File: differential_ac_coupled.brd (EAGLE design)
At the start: 66 x 40.6 mm, 25 parts, among them U1 AD8421

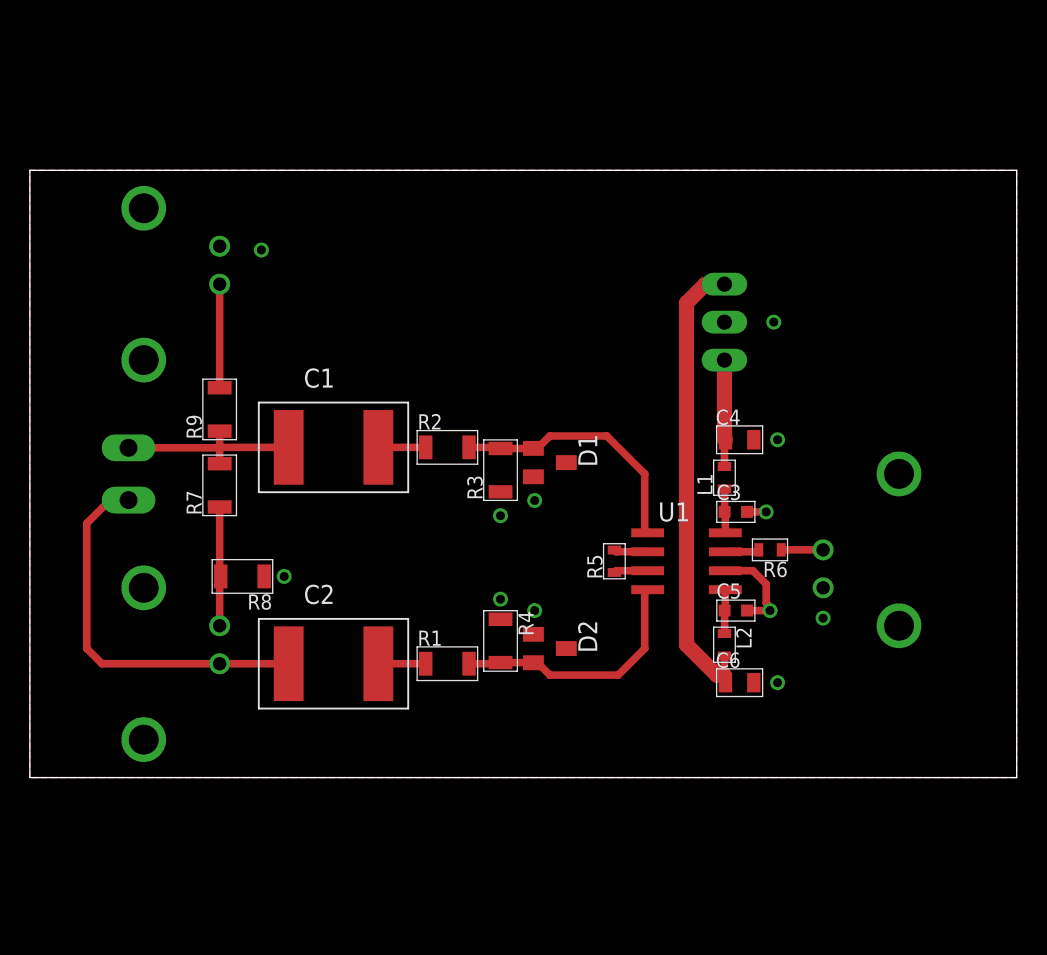
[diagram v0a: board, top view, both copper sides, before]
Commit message: Add battery holders
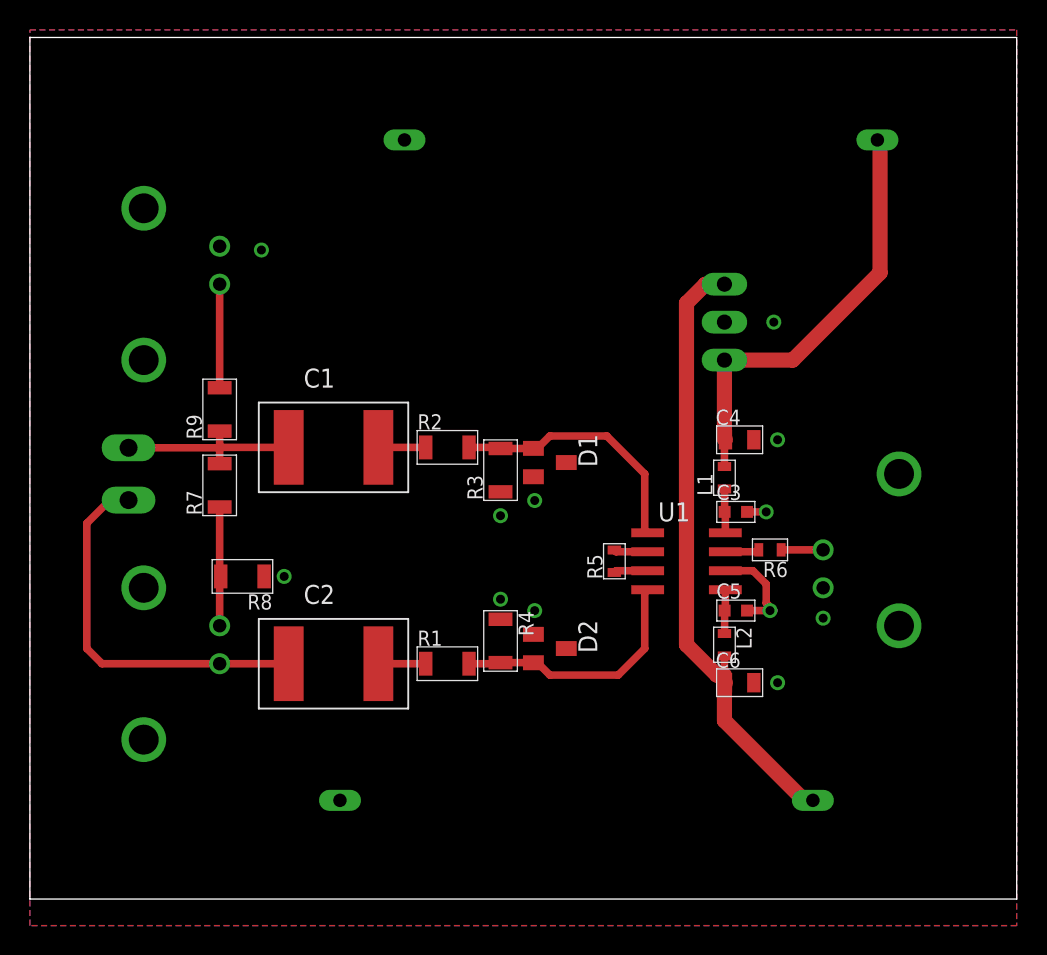
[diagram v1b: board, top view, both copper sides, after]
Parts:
- added U$1, U$2: BATT-HOLDER, regulator-jqi:BH23A-BATT-HOLDER
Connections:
- net GND: now also U$1.P$2-, U$2.P$1+
- net V+: now also U$1.P$1+
- net V-: now also U$2.P$2-
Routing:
- net V+: track 7.18 -> 29.0 mm
- net V-: track 31.1 -> 41.8 mm
- net GND: vias 2 -> 11
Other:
- board size 66 x 40.6 mm -> 66 x 57.7 mm
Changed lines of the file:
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@@
 <?xml version="1.0" encoding="utf-8"?>
 <!DOCTYPE eagle SYSTEM "eagle.dtd">
-<eagle version="6.6.0">
+<eagle version="6.5.0">
 <drawing>
 <settings>
@@
 <board>
 <plain>
-<wire x1="0" y1="40.64" x2="0" y2="0" width="0" layer="20"/>
-<wire x1="0" y1="0" x2="66.04" y2="0" width="0" layer="20"/>
-<wire x1="66.04" y1="0" x2="66.04" y2="40.64" width="0" layer="20"/>
-<wire x1="66.04" y1="40.64" x2="0" y2="40.64" width="0" layer="20"/>
+<wire x1="0" y1="49.53" x2="0" y2="-8.128" width="0" layer="20"/>
+<wire x1="0" y1="-8.128" x2="66.04" y2="-8.128" width="0" layer="20"/>
+<wire x1="66.04" y1="-8.128" x2="66.04" y2="49.53" width="0" layer="20"/>
+<wire x1="66.04" y1="49.53" x2="0" y2="49.53" width="0" layer="20"/>
 </plain>
 <attributes>
@@
 <element name="R8" library="jqi_passives" package="R_1206" value="" x="14.224" y="13.462" rot="R180"/>
 <element name="R9" library="jqi_passives" package="R_1206" value="0R" x="12.7" y="24.638" rot="R90"/>
+<element name="U$1" library="regulator-jqi" package="BH23A-BATT-HOLDER" value="BATT-HOLDER" x="40.894" y="42.672" rot="MR0">
+<attribute name="DIGIKEY" value="BH23APC-ND" x="40.894" y="42.672" size="1.778" layer="28" rot="MR0" display="off"/>
+</element>
+<element name="U$2" library="regulator-jqi" package="BH23A-BATT-HOLDER" value="BATT-HOLDER" x="36.576" y="-1.524" rot="MR180">
+<attribute name="DIGIKEY" value="BH23APC-ND" x="36.576" y="-1.524" size="1.778" layer="28" rot="MR180" display="off"/>
+</element>
 </elements>
 <signals>
@@
 <contactref element="IN-" pad="2"/>
 <contactref element="R8" pad="P$1"/>
-<polygon width="0.254" layer="1" isolate="1.27" thermals="no">
-<vertex x="0" y="40.64"/>
-<vertex x="66.04" y="40.64"/>
-<vertex x="66.04" y="0"/>
-<vertex x="0" y="0"/>
+<polygon width="0.254" layer="1" isolate="1.27">
+<vertex x="0" y="50.038"/>
+<vertex x="66.04" y="50.038"/>
+<vertex x="66.04" y="-9.906"/>
+<vertex x="0" y="-9.906"/>
 </polygon>
 <wire x1="46.542" y1="13.843" x2="48.387" y2="13.843" width="0.508" layer="1"/>
@@
 <wire x1="47.994" y1="17.78" x2="49.276" y2="17.78" width="0.508" layer="1"/>
 <polygon width="0.4064" layer="16">
-<vertex x="0" y="40.64"/>
-<vertex x="66.04" y="40.64"/>
-<vertex x="66.04" y="0"/>
-<vertex x="0" y="0"/>
+<vertex x="0" y="50.038"/>
+<vertex x="66.04" y="50.038"/>
+<vertex x="66.04" y="-9.906"/>
+<vertex x="0" y="-9.906"/>
 </polygon>
 <via x="49.276" y="17.78" extent="1-16" drill="0.6"/>
 <via x="49.53" y="11.176" extent="1-16" drill="0.6"/>
+<contactref element="U$1" pad="P$2-"/>
+<contactref element="U$2" pad="P$1+"/>
+<via x="50.038" y="22.606" extent="1-16" drill="0.6"/>
+<via x="33.782" y="18.542" extent="1-16" drill="0.6"/>
+<via x="31.496" y="17.526" extent="1-16" drill="0.6"/>
+<via x="33.782" y="11.176" extent="1-16" drill="0.6"/>
+<via x="31.496" y="11.938" extent="1-16" drill="0.6"/>
+<via x="50.038" y="6.35" extent="1-16" drill="0.6"/>
+<via x="53.086" y="10.668" extent="1-16" drill="0.6"/>
+<via x="49.784" y="30.48" extent="1-16" drill="0.6"/>
+<via x="17.018" y="13.462" extent="1-16" drill="0.6"/>
 </signal>
 <signal name="N$7">
@@
 <wire x1="43.942" y1="31.75" x2="45.212" y2="33.02" width="1.016" layer="1"/>
 <wire x1="45.212" y1="33.02" x2="46.482" y2="33.02" width="1.016" layer="1"/>
+<contactref element="U$2" pad="P$2-"/>
+<wire x1="52.4002" y1="-1.524" x2="51.816" y2="-1.524" width="1.016" layer="1"/>
+<wire x1="51.816" y1="-1.524" x2="46.482" y2="3.81" width="1.016" layer="1"/>
+<wire x1="46.482" y1="3.81" x2="46.482" y2="6.284" width="1.016" layer="1"/>
+<wire x1="46.482" y1="6.284" x2="46.548" y2="6.35" width="1.016" layer="1"/>
 </signal>
 <signal name="V+">
@@
 <wire x1="46.482" y1="27.94" x2="46.482" y2="22.672" width="1.016" layer="1"/>
 <wire x1="46.482" y1="22.672" x2="46.548" y2="22.606" width="1.016" layer="1"/>
+<contactref element="U$1" pad="P$1+"/>
+<wire x1="46.482" y1="27.94" x2="51.054" y2="27.94" width="1.016" layer="1"/>
+<wire x1="51.054" y1="27.94" x2="56.896" y2="33.782" width="1.016" layer="1"/>
+<wire x1="56.896" y1="33.782" x2="56.896" y2="42.4942" width="1.016" layer="1"/>
+<wire x1="56.896" y1="42.4942" x2="56.7182" y2="42.672" width="1.016" layer="1"/>
 </signal>
 <signal name="N$5">
@@
 <wire x1="12.7" y1="13.388" x2="12.774" y2="13.462" width="0.508" layer="1"/>
 </signal>
-<signal name="N$15">
-<via x="31.496" y="17.526" extent="1-16" drill="0.6"/>
-</signal>
-<signal name="N$16">
-<via x="31.496" y="11.938" extent="1-16" drill="0.6"/>
-</signal>
-<signal name="N$17">
-<via x="33.782" y="11.176" extent="1-16" drill="0.6"/>
-</signal>
-<signal name="N$18">
-<via x="33.782" y="18.542" extent="1-16" drill="0.6"/>
-</signal>
-<signal name="N$19">
-<via x="50.038" y="22.606" extent="1-16" drill="0.6"/>
-</signal>
-<signal name="N$20">
-<via x="50.038" y="6.35" extent="1-16" drill="0.6"/>
-</signal>
 <signal name="N$21">
 <via x="15.494" y="35.306" extent="1-16" drill="0.6"/>
 </signal>
-<signal name="N$22">
-<via x="17.018" y="13.462" extent="1-16" drill="0.6"/>
-</signal>
-<signal name="N$23">
-<via x="53.086" y="10.668" extent="1-16" drill="0.6"/>
-</signal>
-<signal name="N$24">
-<via x="49.784" y="30.48" extent="1-16" drill="0.6"/>
-</signal>
 </signals>
